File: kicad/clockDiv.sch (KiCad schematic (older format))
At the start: 8 parts

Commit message: add schmitt trigger and power input
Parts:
- added D?: LED, symbol Device:LED
- added J?: Conn_02x05_Counter_Clockwise, symbol Connector_Generic:Conn_02x05_Counter_Clockwise
- added J?: AudioJack2, symbol Connector:AudioJack2
- added R?: R, symbol Device:R
- added SW?: SW_Push, symbol Switch:SW_Push
- added U?: LM7805_TO220, Package_TO_SOT_THT:TO-220-3_Vertical, symbol Regulator_Linear:LM7805_TO220
- added U?: SN74HC14N, DIP254P762X508-14, symbol SN74HC14N:SN74HC14N
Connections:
- net +5V: now also U?.3 (VO)
- net DIV1: now also R?.2
- net GND: now also J?.2 (Pin_2), J?.3 (Pin_3), J?.4 (Pin_4), J?.7 (Pin_7), J?.8 (Pin_8), J?.9 (Pin_9), U?.2 (GND)
- new net: D?.2 (A), R?.1
- new net +12V: J?.1 (Pin_1), J?.10 (Pin_10), U?.1 (VI)
- no-connect marks 0 -> 2
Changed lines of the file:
@@
 $EndComp
 $Comp
-L power:GND #PWR?
+L power:GND #PWR0101
 U 1 1 5EFF1BEB
 P 7450 3400
-F 0 "#PWR?" H 7450 3150 50  0001 C CNN
+F 0 "#PWR0101" H 7450 3150 50  0001 C CNN
 F 1 "GND" H 7455 3227 50  0000 C CNN
 F 2 "" H 7450 3400 50  0001 C CNN
@@
 $EndComp
 $Comp
-L power:GND #PWR?
+L power:GND #PWR0102
 U 1 1 5EFF1F3B
 P 5150 5300
-F 0 "#PWR?" H 5150 5050 50  0001 C CNN
+F 0 "#PWR0102" H 5150 5050 50  0001 C CNN
 F 1 "GND" H 5155 5127 50  0000 C CNN
 F 2 "" H 5150 5300 50  0001 C CNN
@@
 $EndComp
 $Comp
-L power:+5V #PWR?
+L power:+5V #PWR0103
 U 1 1 5EFF2E09
 P 5150 2300
-F 0 "#PWR?" H 5150 2150 50  0001 C CNN
+F 0 "#PWR0103" H 5150 2150 50  0001 C CNN
 F 1 "+5V" H 5165 2473 50  0000 C CNN
 F 2 "" H 5150 2300 50  0001 C CNN
@@
 $EndComp
 $Comp
-L power:+5V #PWR?
+L power:+5V #PWR0104
 U 1 1 5EFF32A5
 P 7450 2500
-F 0 "#PWR?" H 7450 2350 50  0001 C CNN
+F 0 "#PWR0104" H 7450 2350 50  0001 C CNN
 F 1 "+5V" H 7465 2673 50  0000 C CNN
 F 2 "" H 7450 2500 50  0001 C CNN
@@
 $EndComp
 $Comp
-L power:+5V #PWR?
+L power:+5V #PWR0105
 U 1 1 5F00737D
 P 2100 1000
-F 0 "#PWR?" H 2100 850 50  0001 C CNN
+F 0 "#PWR0105" H 2100 850 50  0001 C CNN
 F 1 "+5V" H 2115 1173 50  0000 C CNN
 F 2 "" H 2100 1000 50  0001 C CNN
@@
 Connection ~ 2100 1400
 $Comp
-L power:GND #PWR?
+L power:GND #PWR0106
 U 1 1 5F00A598
 P 2100 1700
-F 0 "#PWR?" H 2100 1450 50  0001 C CNN
+F 0 "#PWR0106" H 2100 1450 50  0001 C CNN
 F 1 "GND" H 2105 1527 50  0000 C CNN
 F 2 "" H 2100 1700 50  0001 C CNN
@@
 $EndComp
 $Comp
-L power:GND #PWR?
+L power:GND #PWR0107
 U 1 1 5F00A991
 P 1550 1500
-F 0 "#PWR?" H 1550 1250 50  0001 C CNN
+F 0 "#PWR0107" H 1550 1250 50  0001 C CNN
 F 1 "GND" H 1555 1327 50  0000 C CNN
 F 2 "" H 1550 1500 50  0001 C CNN
@@
 $EndComp
 $Comp
-L power:GND #PWR?
+L power:GND #PWR0108
 U 1 1 5F00FC2B
 P 1000 1100
-F 0 "#PWR?" H 1000 850 50  0001 C CNN
+F 0 "#PWR0108" H 1000 850 50  0001 C CNN
 F 1 "GND" V 1005 972 50  0000 R CNN
 F 2 "" H 1000 1100 50  0001 C CNN
@@
 Wire Wire Line
 	1000 1200 1250 1200
+$Comp
+L Regulator_Linear:LM7805_TO220 U?
+U 1 1 5EFF7CC6
+P 1550 3600
+F 0 "U?" H 1550 3842 50  0000 C CNN
+F 1 "LM7805_TO220" H 1550 3751 50  0000 C CNN
+F 2 "Package_TO_SOT_THT:TO-220-3_Vertical" H 1550 3825 50  0001 C CIN
+F 3 "http://www.fairchildsemi.com/ds/LM/LM7805.pdf" H 1550 3550 50  0001 C CNN
+	1    1550 3600
+	1    0    0    -1
+$EndComp
+$Comp
+L Connector_Generic:Conn_02x05_Counter_Clockwise J?
+U 1 1 5EFF94FC
+P 1100 4650
+F 0 "J?" H 1150 5067 50  0000 C CNN
+F 1 "Conn_02x05_Counter_Clockwise" H 1150 4976 50  0000 C CNN
+F 2 "" H 1100 4650 50  0001 C CNN
+F 3 "~" H 1100 4650 50  0001 C CNN
+	1    1100 4650
+	1    0    0    -1
+$EndComp
+$Comp
+L power:+12V #PWR?
+U 1 1 5EFFA56E
+P 1400 4450
+F 0 "#PWR?" H 1400 4300 50  0001 C CNN
+F 1 "+12V" V 1415 4578 50  0000 L CNN
+F 2 "" H 1400 4450 50  0001 C CNN
+F 3 "" H 1400 4450 50  0001 C CNN
+	1    1400 4450
+	0    1    1    0
+$EndComp
+$Comp
+L power:GND #PWR?
+U 1 1 5EFFAD03
+P 1450 4650
+F 0 "#PWR?" H 1450 4400 50  0001 C CNN
+F 1 "GND" V 1455 4522 50  0000 R CNN
+F 2 "" H 1450 4650 50  0001 C CNN
+F 3 "" H 1450 4650 50  0001 C CNN
+	1    1450 4650
+	0    -1   -1   0
+$EndComp
+Wire Wire Line
+	1400 4650 1450 4650
+Wire Wire Line
+	1400 4550 1400 4650
+Connection ~ 1400 4650
+Wire Wire Line
+	1400 4650 1400 4750
+$Comp
+L power:+12V #PWR?
+U 1 1 5EFFC209
+P 1250 3600
+F 0 "#PWR?" H 1250 3450 50  0001 C CNN
+F 1 "+12V" V 1265 3728 50  0000 L CNN
+F 2 "" H 1250 3600 50  0001 C CNN
+F 3 "" H 1250 3600 50  0001 C CNN
+	1    1250 3600
+	0    -1   -1   0
+$EndComp
+$Comp
+L power:GND #PWR?
+U 1 1 5EFFCD3F
+P 1550 3900
+F 0 "#PWR?" H 1550 3650 50  0001 C CNN
+F 1 "GND" H 1555 3727 50  0000 C CNN
+F 2 "" H 1550 3900 50  0001 C CNN
+F 3 "" H 1550 3900 50  0001 C CNN
+	1    1550 3900
+	1    0    0    -1
+$EndComp
+$Comp
+L power:+5V #PWR?
+U 1 1 5EFFD289
+P 1850 3600
+F 0 "#PWR?" H 1850 3450 50  0001 C CNN
+F 1 "+5V" V 1865 3728 50  0000 L CNN
+F 2 "" H 1850 3600 50  0001 C CNN
+F 3 "" H 1850 3600 50  0001 C CNN
+	1    1850 3600
+	0    1    1    0
+$EndComp
+NoConn ~ 1400 4850
+NoConn ~ 900  4850
+$Comp
+L power:GND #PWR?
+U 1 1 5EFFE68B
+P 850 4650
+F 0 "#PWR?" H 850 4400 50  0001 C CNN
+F 1 "GND" V 855 4522 50  0000 R CNN
+F 2 "" H 850 4650 50  0001 C CNN
+F 3 "" H 850 4650 50  0001 C CNN
+	1    850  4650
+	0    1    1    0
+$EndComp
+$Comp
+L power:+12V #PWR?
+U 1 1 5EFFECA8
+P 900 4450
+F 0 "#PWR?" H 900 4300 50  0001 C CNN
+F 1 "+12V" V 915 4578 50  0000 L CNN
+F 2 "" H 900 4450 50  0001 C CNN
+F 3 "" H 900 4450 50  0001 C CNN
+	1    900  4450
+	0    -1   -1   0
+$EndComp
+Wire Wire Line
+	900  4550 900  4650
+Wire Wire Line
+	900  4650 900  4750
+Connection ~ 900  4650
+Wire Wire Line
+	900  4650 850  4650
+Text GLabel 7200 5450 0    50   Input ~ 0
+DIV1
+$Comp
+L Device:LED D?
+U 1 1 5F00833A
+P 7250 4950
+F 0 "D?" V 7197 5030 50  0000 L CNN
+F 1 "LED" V 7288 5030 50  0000 L CNN
+F 2 "" H 7250 4950 50  0001 C CNN
+F 3 "~" H 7250 4950 50  0001 C CNN
+	1    7250 4950
+	0    1    1    0
+$EndComp
+$Comp
+L Device:R R?
+U 1 1 5F008F83
+P 7250 5250
+F 0 "R?" H 7320 5296 50  0000 L CNN
+F 1 "R" H 7320 5205 50  0000 L CNN
+F 2 "" V 7180 5250 50  0001 C CNN
+F 3 "~" H 7250 5250 50  0001 C CNN
+	1    7250 5250
+	1    0    0    -1
+$EndComp
+$Comp
+L Connector:AudioJack2 J?
+U 1 1 5F011064
+P 8050 5400
+F 0 "J?" H 8082 5725 50  0000 C CNN
+F 1 "AudioJack2" H 8082 5634 50  0000 C CNN
+F 2 "" H 8050 5400 50  0001 C CNN
+F 3 "~" H 8050 5400 50  0001 C CNN
+	1    8050 5400
+	-1   0    0    1
+$EndComp
+$Comp
+L power:GND #PWR?
+U 1 1 5F01169D
+P 7700 5600
+F 0 "#PWR?" H 7700 5350 50  0001 C CNN
+F 1 "GND" H 7705 5427 50  0000 C CNN
+F 2 "" H 7700 5600 50  0001 C CNN
+F 3 "" H 7700 5600 50  0001 C CNN
+	1    7700 5600
+	1    0    0    -1
+$EndComp
+Wire Wire Line
+	7200 5450 7250 5450
+Wire Wire Line
+	7250 5450 7250 5400
+$Comp
+L Switch:SW_Push SW?
+U 1 1 5F0139B4
+P 8900 4450
+F 0 "SW?" H 8900 4735 50  0000 C CNN
+F 1 "SW_Push" H 8900 4644 50  0000 C CNN
+F 2 "" H 8900 4650 50  0001 C CNN
+F 3 "~" H 8900 4650 50  0001 C CNN
+	1    8900 4450
+	1    0    0    -1
+$EndComp
+$Comp
+L SN74HC14N:SN74HC14N U?
+U 1 1 5F009183
+P 3600 6500
+F 0 "U?" H 3600 7170 50  0000 C CNN
+F 1 "SN74HC14N" H 3600 7079 50  0000 C CNN
+F 2 "DIP254P762X508-14" H 3600 6500 50  0001 L BNN
+F 3 "Texas Instruments" H 3600 6500 50  0001 L BNN
+F 4 "9591125" H 3600 6500 50  0001 L BNN "Field4"
+F 5 "60K6826" H 3600 6500 50  0001 L BNN "Field5"
+F 6 "SN74HC14N" H 3600 6500 50  0001 L BNN "Field6"
+F 7 "DIP-14" H 3600 6500 50  0001 L BNN "Field7"
+	1    3600 6500
+	1    0    0    -1
+$EndComp
 $EndSCHEMATC

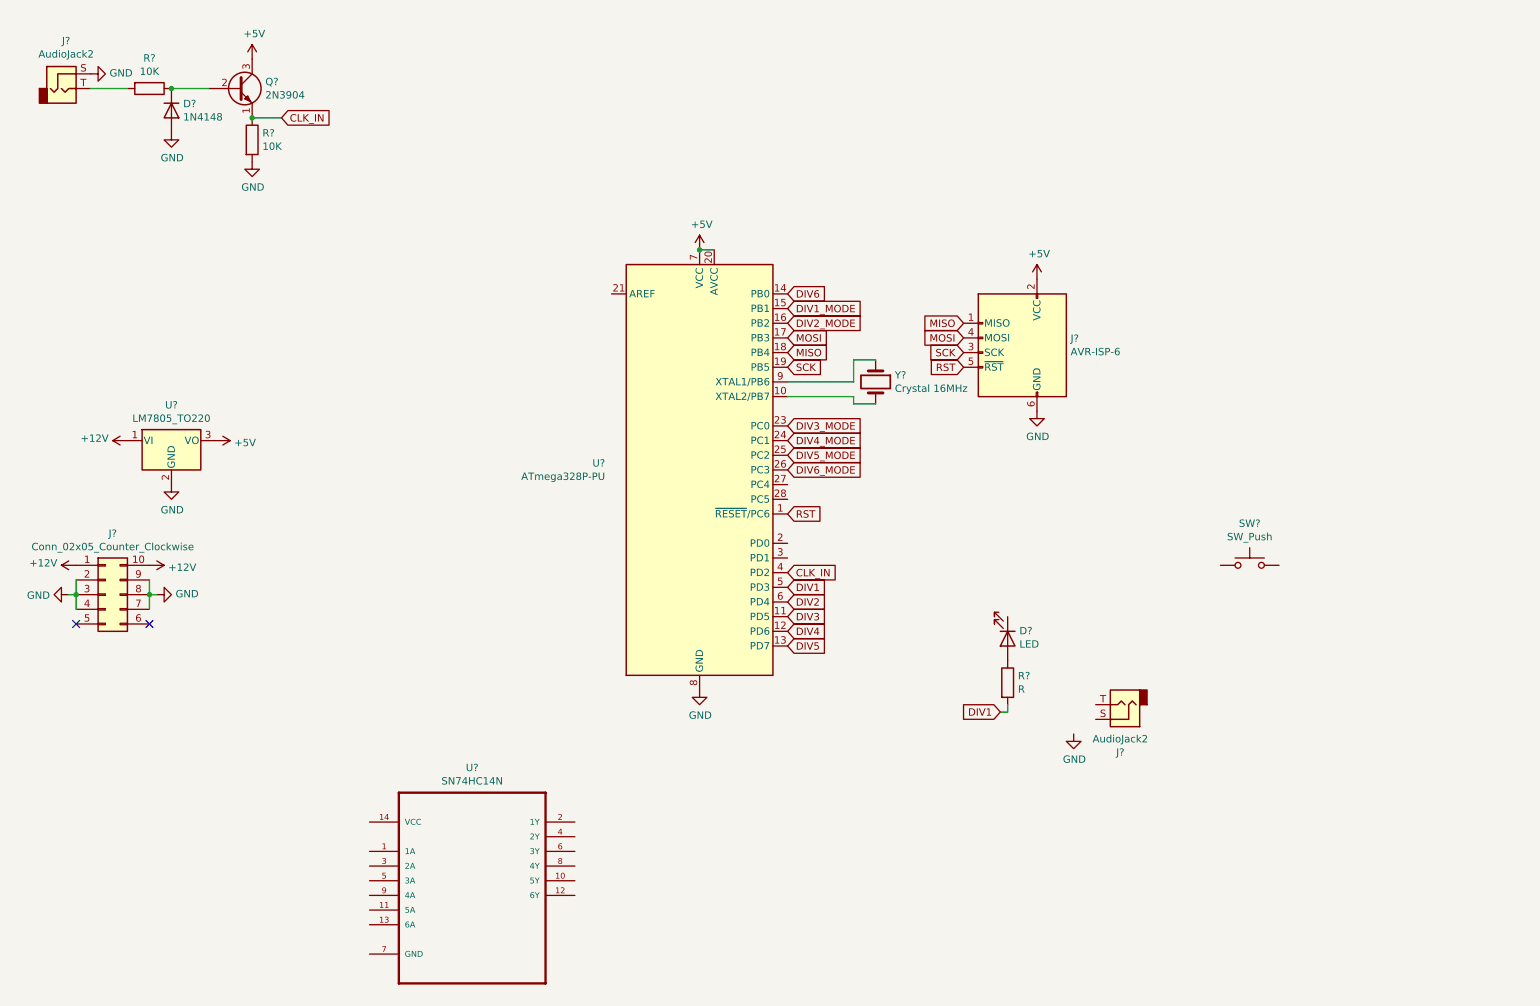
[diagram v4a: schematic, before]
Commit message: use 2 schmitt triggers to invert the inverted signal(high=high)
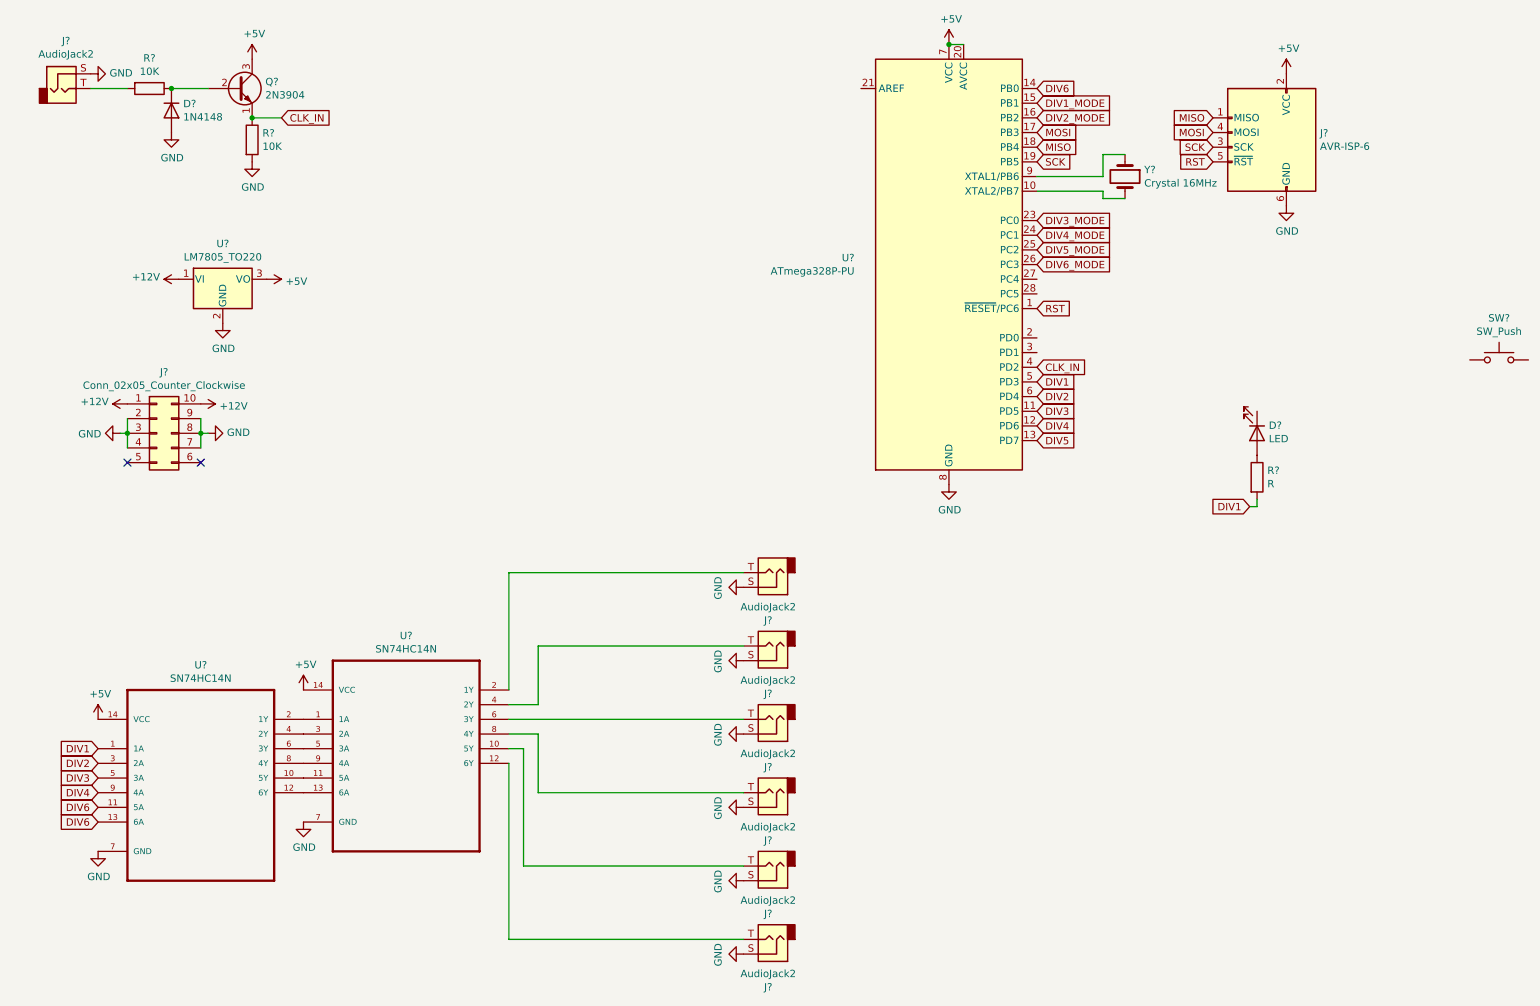
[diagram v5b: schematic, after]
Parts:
- added J? (x5): AudioJack2, symbol Connector:AudioJack2
- added U?: SN74HC14N, DIP254P762X508-14, symbol SN74HC14N:SN74HC14N
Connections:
- net +5V: now also U?.14 (VCC), U?.14 (VCC)
- net DIV1: now also U?.1 (1A)
- net DIV2: now also U?.3 (2A)
- net DIV3: now also U?.5 (3A)
- net DIV4: now also U?.9 (4A)
- net DIV6: now also U?.11 (5A), U?.13 (6A)
- net GND: now also J?.S, U?.7 (GND), J?.S, J?.S, J?.S, J?.S, J?.S, U?.7 (GND)
- net at U?.10 (5Y): now also U?.11 (5A)
- net at U?.12 (6Y): now also U?.13 (6A)
- net at U?.2 (1Y): now also U?.1 (1A)
- net at U?.4 (2Y): now also U?.3 (2A)
- net at U?.6 (3Y): now also U?.5 (3A)
- net at U?.8 (4Y): now also U?.9 (4A)
- net at J?.T: now also U?.2 (1Y)
- new net: J?.T, U?.10 (5Y)
- new net: J?.T, U?.12 (6Y)
- new net: J?.T, U?.4 (2Y)
- new net: J?.T, U?.6 (3Y)
- new net: J?.T, U?.8 (4Y)
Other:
- moved on the sheet: D?, J?, R?, SW?, U?, Y?
